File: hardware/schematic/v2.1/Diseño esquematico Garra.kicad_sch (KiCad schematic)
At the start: 20 parts

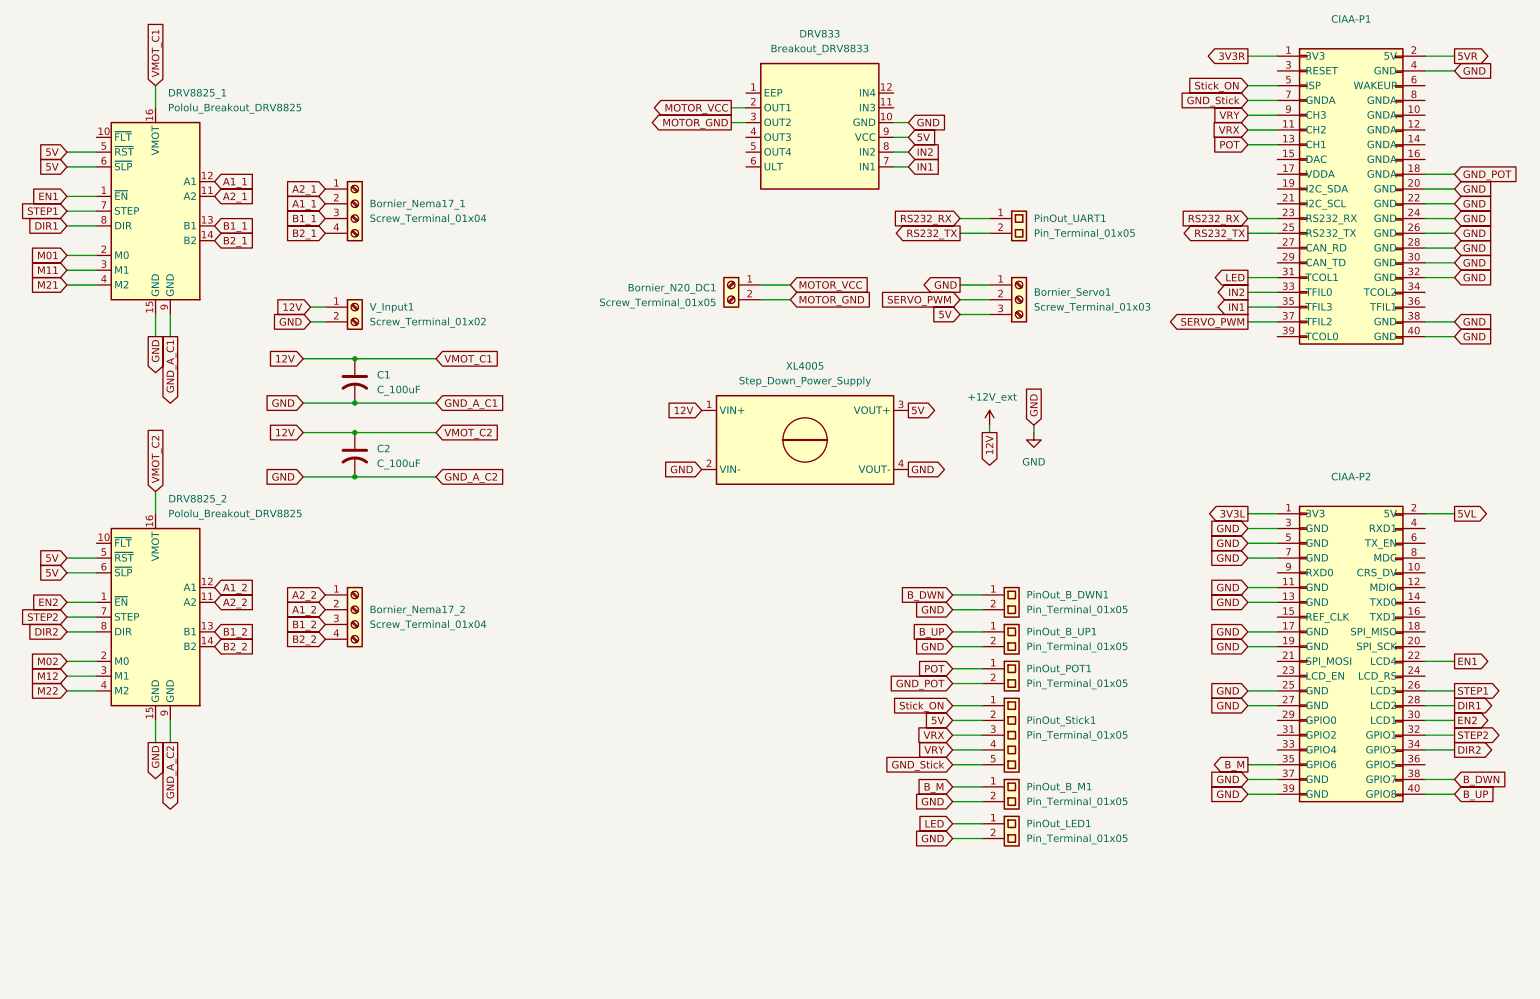
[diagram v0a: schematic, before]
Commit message: Pcb branch (#11)
* refactor

* feat: PCB routing first stage completed

* docs: Schematics PDF added

* fix: PCB border colision

* feat: Copper layers added to the PCB

* feat: New PCB design with new components [LED, B_M]

* feat: add through holes for connectivity & GNDs links

* feat: hole diameter adjustment

* fix: PDF

* feat: change route system in PCB

* feat: add new esp32 schematic

* feat: complete PCB

* feat: take png and pdf from finished schematic

* feat: valid pdf PCB template

* fix: Expand PCB routes and copper holes

---------

Co-authored-by: ManuSavenia <saveniamanuel@egmail.com>
Co-authored-by: Iván Valentín Polanis <polanis.ivan@alu.ing.unlp.edu.ar>
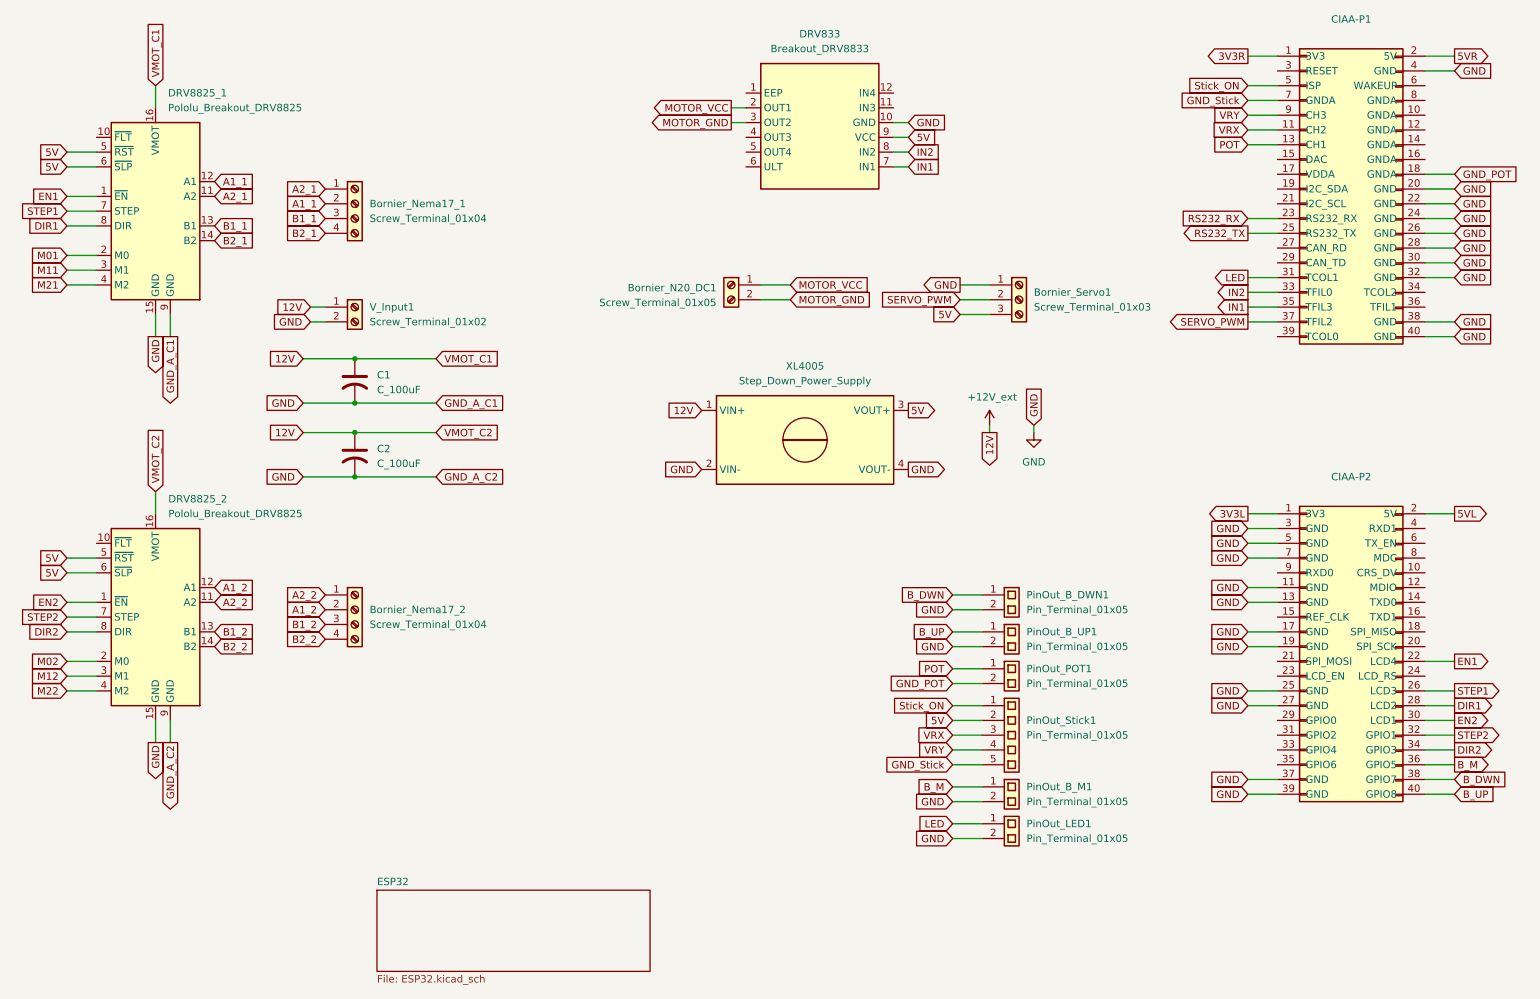
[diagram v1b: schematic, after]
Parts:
- removed PinOut_UART1: Pin_Terminal_01x05, Connector_PinSocket_2.00mm:PinSocket_1x02_P2.00mm_Vertical, symbol Connector:Screw_Terminal_01x02
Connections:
- net B_M: now also CIAA-P2.36 (GPIO5); no longer CIAA-P2.35 (GPIO6)
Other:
- added sheet ESP32 (ESP32.kicad_sch)
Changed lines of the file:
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@@
 	(wire
 		(pts
-			(xy 184.15 49.53) (xy 189.23 49.53)
-		)
-		(stroke
-			(width 0)
-			(type default)
-		)
-	)
-	(wire
-		(pts
 			(xy 30.48 45.72) (xy 35.56 45.72)
 		)
@@
 	(wire
 		(pts
+			(xy 264.16 143.51) (xy 269.24 143.51)
+		)
+		(stroke
+			(width 0)
+			(type default)
+		)
+	)
+	(wire
+		(pts
 			(xy 48.26 69.85) (xy 48.26 66.04)
 		)
@@
 	(wire
 		(pts
-			(xy 184.15 52.07) (xy 189.23 52.07)
-		)
-		(stroke
-			(width 0)
-			(type default)
-		)
-	)
-	(wire
-		(pts
 			(xy 30.48 125.73) (xy 35.56 125.73)
 		)
@@
 	(wire
 		(pts
-			(xy 233.68 143.51) (xy 238.76 143.51)
-		)
-		(stroke
-			(width 0)
-			(type default)
-		)
-	)
-	(wire
-		(pts
 			(xy 80.01 93.98) (xy 93.98 93.98)
 		)
@@
 		)
 	)
-	(global_label "RS232_TX"
-		(shape output)
-		(at 184.15 52.07 180)
-		(effects
-			(font
-				(size 1.27 1.27)
-			)
-			(justify right)
-		)
-		(property "Intersheetrefs" "${INTERSHEET_REFS}"
-			(at 184.15 52.07 0)
-			(effects
-				(font
-					(size 1.27 1.27)
-				)
-				(hide yes)
-			)
-		)
-	)
 	(global_label "GND"
 		(shape input)
@@
 		)
 	)
-	(global_label "RS232_RX"
-		(shape input)
-		(at 184.15 49.53 180)
-		(effects
-			(font
-				(size 1.27 1.27)
-			)
-			(justify right)
-		)
-		(property "Intersheetrefs" "${INTERSHEET_REFS}"
-			(at 184.15 49.53 0)
-			(effects
-				(font
-					(size 1.27 1.27)
-				)
-				(hide yes)
-			)
-		)
-	)
 	(global_label "GND"
 		(shape output)
@@
 	(global_label "B_M"
 		(shape output)
-		(at 233.68 143.51 180)
+		(at 269.24 143.51 0)
 		(effects
 			(font
 				(size 1.27 1.27)
 			)
-			(justify right)
+			(justify left)
 		)
 		(property "Intersheetrefs" "${INTERSHEET_REFS}"
-			(at 233.68 143.51 0)
+			(at 269.24 143.51 0)
 			(effects
 				(font
@@
 	)
 	(symbol
-		(lib_name "Screw_Terminal_01x02_3")
-		(lib_id "Connector:Screw_Terminal_01x02")
-		(at 194.31 49.53 0)
-		(unit 1)
-		(exclude_from_sim no)
-		(in_bom yes)
-		(on_board yes)
-		(dnp no)
-		(fields_autoplaced yes)
-		(property "Reference" "PinOut_UART1"
-			(at 196.85 49.5299 0)
-			(effects
-				(font
-					(size 1.27 1.27)
-				)
-				(justify left)
-			)
-		)
-		(property "Value" "Pin_Terminal_01x05"
-			(at 196.85 52.0699 0)
-			(effects
-				(font
-					(size 1.27 1.27)
-				)
-				(justify left)
-			)
-		)
-		(property "Footprint" "Connector_PinSocket_2.00mm:PinSocket_1x02_P2.00mm_Vertical"
-			(at 194.564 44.196 0)
-			(effects
-				(font
-					(size 1.27 1.27)
-				)
-				(hide yes)
-			)
-		)
-		(property "Datasheet" "~"
-			(at 195.834 54.102 0)
-			(effects
-				(font
-					(size 1.27 1.27)
-				)
-				(hide yes)
-			)
-		)
-		(property "Description" "Generic screw terminal, single row, 01x02, script generated (kicad-library-utils/schlib/autogen/connector/)"
-			(at 194.818 55.118 0)
-			(effects
-				(font
-					(size 1.27 1.27)
-				)
-				(hide yes)
-			)
-		)
-		(pin "2"
-		)
-		(pin "1"
-		)
-		(instances
-			(project "Diseño esquematico Garra"
-				(path "/a88248f6-7b70-4a9d-b538-4e8e42a3a066"
-					(reference "PinOut_UART1")
-					(unit 1)
-				)
-			)
-		)
-	)
-	(symbol
 		(lib_id "Connector:Screw_Terminal_01x02")
 		(at 80.01 64.77 0)
@@
 				)
 			)
+		)
+	)
+	(sheet
+		(at 83.82 165.1)
+		(size 46.99 13.97)
+		(exclude_from_sim no)
+		(in_bom yes)
+		(on_board yes)
+		(dnp no)
+		(fields_autoplaced yes)
+		(stroke
+			(width 0.1524)
+			(type solid)
+		)
+		(fill
+			(color 0 0 0 0.0000)
+		)
+		(property "Sheetname" "ESP32"
+			(at 83.82 164.3884 0)
+			(effects
+				(font
+					(size 1.27 1.27)
+				)
+				(justify left bottom)
+			)
+		)
+		(property "Sheetfile" "ESP32.kicad_sch"
+			(at 83.82 179.6546 0)
+			(effects
+				(font
+					(size 1.27 1.27)
+				)
+				(justify left top)
+			)
+		)
+		(instances
+			(project "Diseño esquematico Garra"
+				(path "/a88248f6-7b70-4a9d-b538-4e8e42a3a066"
+					(page "2")
+				)
+			)
